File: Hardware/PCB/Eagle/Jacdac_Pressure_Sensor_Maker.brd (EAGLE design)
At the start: 27.9 x 27.9 mm, 31 parts, among them J1 JACDAC_EDGE_CONN-INNIE, J2 SWD-ADAPTER-, J3 HEADER_MALE-1X07, U1 NCP114ASN330T1G, U2 STM32F042F6P6, U3 BAT54S,235, U4 LPS33HWTR

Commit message: Corrected Capacitor values
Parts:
- C5: value 33pF -> 1uF
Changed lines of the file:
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@@
 <attribute name="NAME" x="14.224" y="8.382" size="0.8128" layer="25" ratio="15" rot="R90" align="bottom-center"/>
 </element>
-<element name="C5" library="milador_SMD" library_urn="urn:adsk.eagle:library:27847482" package="0805-MP" package3d_urn="urn:adsk.eagle:package:27847629/3" value="33pF" x="15.24" y="13.462" smashed="yes">
+<element name="C5" library="milador_SMD" library_urn="urn:adsk.eagle:library:27847482" package="0805-MP" package3d_urn="urn:adsk.eagle:package:27847629/3" value="1uF" x="15.24" y="13.462" smashed="yes">
 <attribute name="NAME" x="12.8524" y="12.9286" size="0.8128" layer="25" font="vector" ratio="15" align="bottom-center"/>
 <attribute name="VALUE" x="13.0302" y="12.4968" size="0.8128" layer="27" font="vector" ratio="15" align="top-center"/>

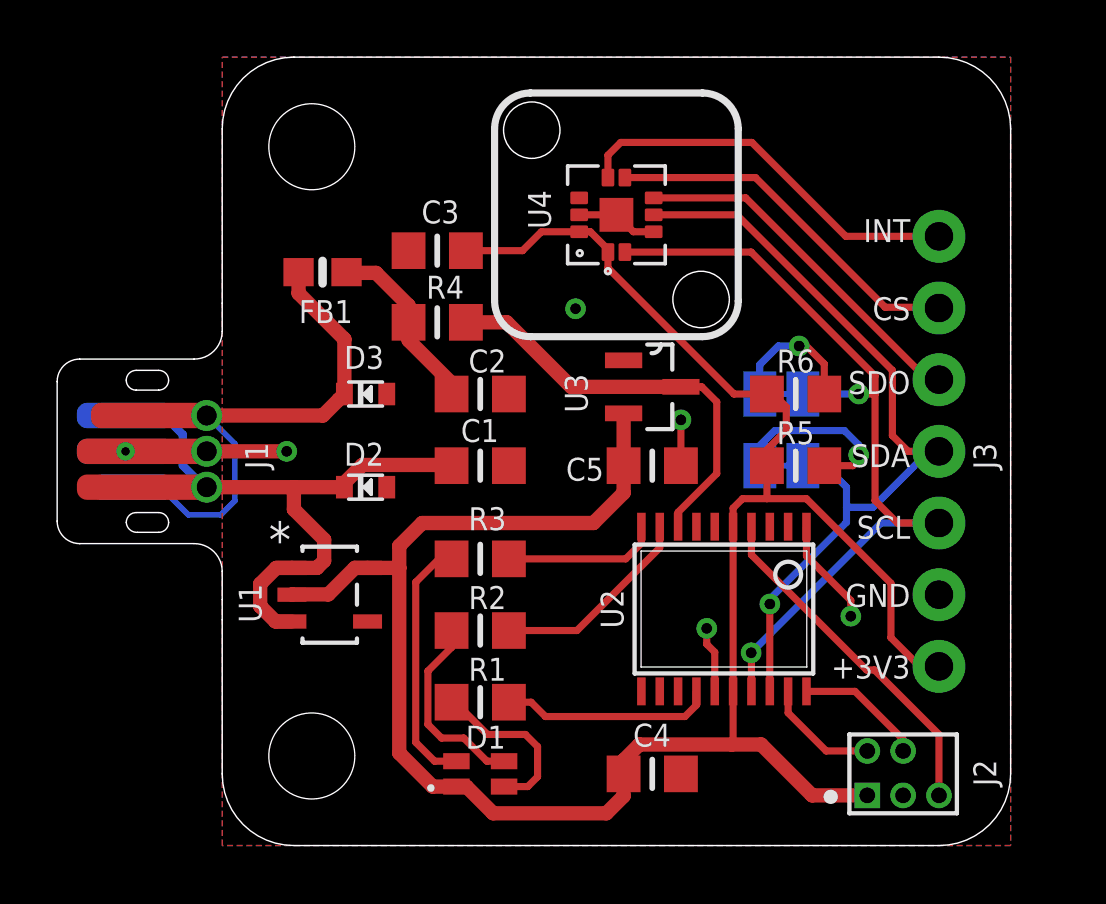
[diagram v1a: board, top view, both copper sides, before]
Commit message: Updated design : Centered Pressure Sensor
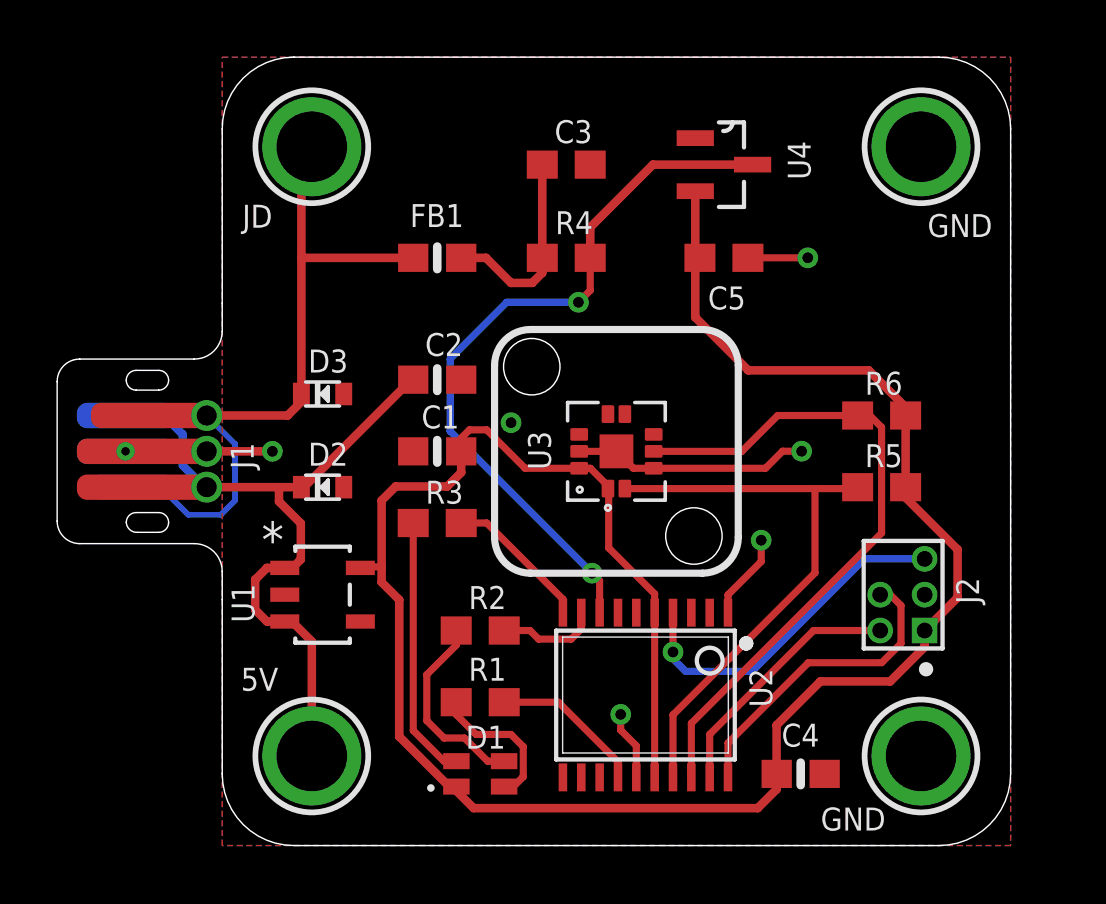
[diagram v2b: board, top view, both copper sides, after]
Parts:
- removed J3: HEADER_MALE-1X07, milador:HEADER_MALE-1X07
- removed JP3: STAND-OFF-3.0, milador:STAND-OFF-3.0
- removed SJ1, SJ2: (no value), milador_SMD:SOLDERJUMPER_CLOSEDWIRE
- removed U$2: MILADOR-PIN-NAME-SCK, milador:PIN-SCK
- removed U$3: MMC-LOGO-SM, MMC Eagle:MMC_SMALL_LOGO
- added H1, H3, H4: MOUNTINGHOLE2.5, milador:MOUNTINGHOLE_2.5_PLATED
- added MMC_LOGO: MMC_LOGO-SM, MMC Eagle:MMC_SMALL_LOGO
- C1: value 1uF -> 0.1uF; device milador_SMD:0805-MP -> milador_SMD:0603-NO
- C2: value 33pF -> 1uF; device milador_SMD:0805-MP -> milador_SMD:0603-NO
- C3: value 0.1uF -> 33pF; device milador_SMD:0805-MP -> milador_SMD:0603
- C4: device milador_SMD:0805-MP -> milador_SMD:0603-NO
- C5, R1, R2, R3, R4, R5, R6: device milador_SMD:0805-MP -> milador_SMD:0603
- H2: value STAND-OFF-3.0 -> MOUNTINGHOLE2.5; device milador:STAND-OFF-3.0 -> milador:MOUNTINGHOLE_2.5_PLATED
- U$1: value MILADOR-PIN-NAME-SDA -> JACDAC-DEVICE-LPS33HW; device milador:PIN-SDA -> milador:JACDAC-LPS33HW
- U3: value BAT54S,235 -> LPS33HWTR; device milador_SMD:SOT23-3 -> milador_SMD:PQFN60P330X330X290-11N
- U4: value LPS33HWTR -> BAT54S,235; device milador_SMD:PQFN60P330X330X290-11N -> milador_SMD:SOT23-3
- moved LABEL2 16.4 mm to (23.1, 18.6)
- moved C5 7.79 mm to (17.8, 20.8)
- moved U$1 6.55 mm to (18.7, 19.8)
- moved J2 6.19 mm to (24.9, 7.62), turned to 90 degrees
- moved C3 5.49 mm to (12.2, 24.1), turned to 0 degrees
- moved C4 5.26 mm to (20.5, 2.54)
- moved R4 5.11 mm to (12.2, 20.8)
- moved U4 4.20 mm to (17.8, 24.1), turned to 0 degrees
- moved U2 4.13 mm to (15.0, 5.33)
- moved FB1 4.10 mm to (7.62, 20.8)
- moved R5 3.14 mm to (23.4, 12.7), turned to 0 degrees
- moved R6 3.14 mm to (23.4, 15.2), turned to 0 degrees
- moved U3 2.62 mm to (14.0, 14.0), turned to 90 degrees
- moved R3 1.98 mm to (7.62, 11.4)
- moved C2 1.61 mm to (7.62, 16.5)
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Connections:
- removed net CS: J3.6, U4.6
- removed net INT: J3.7, U4.7
- removed net N$6: R6.1, SJ1.2
- removed net N$7: R5.1, SJ2.2
- removed net SDO: J3.5, U4.5
- net +3V3: now also C1.1, U3.1, U3.10, U4.2; no longer C3.1, J3.1, U1.2, U3.2, U4.1, U4.10
- net GND: now also H3.P$1, H4.P$1, U1.2, U3.3, U3.8, U3.9, U3.EP, U4.1; no longer J3.2, U3.1, U4.3, U4.8, U4.9, U4.EP
- net JD_DATA: now also U4.3; no longer U3.3
- net J_DATA: now also H2.P$1
- net N$4: now also C3.1; no longer C2.1
- net SCL: now also R5.1, U3.2; no longer J3.3, SJ1.1, U4.2
- net SDA: now also R6.1, U3.4; no longer J3.4, SJ2.1, U4.4
- net VCC: now also C2.1, H1.P$1; no longer C1.1
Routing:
- net INT: track 14.1 -> 0.00 mm
- net CS: track 13.0 -> 0.00 mm
- net SDO: track 12.8 -> 0.00 mm
- net JD_DATA: track 15.0 -> 26.1 mm, vias 0 -> 2
- net SCL: track 30.2 -> 20.6 mm, vias 2 -> 0
- net J_DATA: track 19.8 -> 26.3 mm
- net SWCLK: track 4.54 -> 11.0 mm
- net N$7: track 6.48 -> 0.00 mm, vias 1 -> 0
- net SDA: track 29.3 -> 24.0 mm, vias 1 -> 0
- net SWDIO: track 4.13 -> 9.09 mm
- net GND: track 16.4 -> 21.4 mm, vias 5 -> 6
- net N$6: track 4.93 -> 0.00 mm, vias 1 -> 0
- net VCC: track 23.7 -> 28.1 mm
- net RGB_G: track 7.31 -> 3.58 mm
- net +3V3: track 80.6 -> 77.9 mm
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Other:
- outline, holes or cut-outs redrawn
- board text added: "5V"
- board text added: "JD"
- board text removed: "+3V3"
- board text removed: "CS"
- board text removed: "INT"
- board text removed: "SCL"
- board text removed: "SDA"
- board text removed: "SDO"

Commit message: Added version 1.0
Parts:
- removed D2, D3: RCLAMP0521PATCT, milador_SMD:SOD-523
- removed H1, H2, H3, H4: MOUNTINGHOLE2.5, milador:MOUNTINGHOLE_2.5_PLATED
- removed J1: JACDAC_EDGE_CONN-INNIE, Jacdac:JACDAC-EDGE-CONN-INNIE
- removed LABEL2: JACDAC-DEVICE-PS, milador:JACDAC-PRESSURE-SENSOR
- removed LABEL3: MILADOR-LOGO-, milador:MILADOR_LOGO1
- removed U$1: JACDAC-DEVICE-LPS33HW, milador:JACDAC-LPS33HW
- added J3: 5V, milador:M3-HOLE-PWR-OUTL
- added J4: DATA, milador:M3-HOLE-DATA-NOTCH
- added J5, J6: GND, milador:M3-HOLE-GND
- added JD1, JD2: JACDAC-EDGE-OUTIE, milador:JD-EDGE-OUTIE
- added LABEL_JACDAC_PS: MILADOR-JACDAC-DEVICE-PS, milador:JACDAC-PRESSURE-SENSOR
- added LABEL_LPS33HW: MILADOR-JACDAC-DEVICE-LPS33HW, milador:JACDAC-LPS33HW
- added LABEL_MILADOR: MILADOR-LOGO-, milador:MILADOR_LOGO1
- added LABEL_QR_CODE: MILADOR-QR-CODE-JACDAC-GITHUB-PS, milador:MILADOR_QR_JACDAC_PS
- C1: value 0.1uF -> 1uF
- C2: value 1uF -> 33pF; device milador_SMD:0603-NO -> milador_SMD:0603
- C3: value 33pF -> 1uF; device milador_SMD:0603 -> milador_SMD:0603-NO
- C4: value 1uF -> 0.1uF
- MMC_LOGO: value MMC_LOGO-SM -> MMC_LOGO-XSM; device MMC Eagle:MMC_SMALL_LOGO -> MMC Eagle:MMC_X-SMALL_LOGO
- U1: value NCP114ASN330T1G -> STM32F042F6P6; device milador_SMD:TSOP-5_ONS -> milador_SMD:TSSOP20
- U2: value STM32F042F6P6 -> NCP114ASN330T1G; device milador_SMD:TSSOP20 -> milador_SMD:TSOP-5_ONS
- moved C3 21.8 mm to (17.8, 3.00), turned to 270 degrees
- moved R1 12.1 mm to (9.80, 17.2)
- moved R2 12.1 mm to (9.80, 19.7)
- moved D1 12.0 mm to (9.30, 14.5)
- moved R3 11.0 mm to (9.80, 22.2)
- moved U1 10.1 mm to (12.8, 4.75), turned to 180 degrees
- moved MMC_LOGO 9.48 mm to (12.0, 4.50), turned to 0 degrees
- moved C4 9.13 mm to (18.8, 11.5)
- moved C1 8.49 mm to (8.25, 5.50), turned to 90 degrees
- moved U2 7.90 mm to (9.50, 11.0), turned to 90 degrees
- moved C2 7.42 mm to (14.0, 20.3)
- moved FB1 6.55 mm to (13.8, 23.0)
- moved R6 5.27 mm to (18.5, 17.2)
- moved J2 5.18 mm to (19.9, 6.25)
- moved R5 4.96 mm to (18.8, 14.5)
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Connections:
- net +3V3: now also C3.1, U1.16; no longer C1.1, U2.16
- net GND: now also J5.H, J6.H, JD1.2, JD1.5, JD1.P$2, JD1.P$4, JD2.2, JD2.5, JD2.P$2, JD2.P$4, U1.1, U1.15, U2.2; no longer D2.1, D3.1, H3.P$1, H4.P$1, J1.GND1, J1.GND2, J1.GND3, J1.GND4, U1.2, U2.1, U2.15
- net JD_DATA: now also U1.8; no longer U2.8
- net J_DATA: now also J4.H, JD1.1, JD1.6, JD1.P$3, JD2.1, JD2.6, JD2.P$3; no longer D3.2, H2.P$1, J1.JD1, J1.JD2, J1.JD3
- net N$4: now also C2.1; no longer C3.1
- net RESET: now also U1.4; no longer U2.4
- net RGB_B: now also U1.14; no longer U2.14
- net RGB_G: now also U1.10; no longer U2.9
- net RGB_R: now also U1.9; no longer U2.10
- net SCL: now also U1.17; no longer U2.17
- net SDA: now also U1.18; no longer U2.18
- net SWCLK: now also U1.20; no longer U2.20
- net SWDIO: now also U1.19; no longer U2.19
- net VCC: now also C1.1, J3.H, JD1.3, JD1.4, JD1.P$1, JD2.3, JD2.4, JD2.P$1, U2.1, U2.3; no longer C2.1, D2.2, H1.P$1, J1.VDD1, J1.VDD2, J1.VDD3, U1.1, U1.3
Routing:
- net GND: track 21.4 -> 104.8 mm, vias 6 -> 9
- net +3V3: track 77.9 -> 47.4 mm, vias 0 -> 2
- net J_DATA: track 26.3 -> 51.3 mm, vias 0 -> 5
- net VCC: track 28.1 -> 48.4 mm
- net RGB_R: track 5.20 -> 21.0 mm, vias 0 -> 2
- net RGB_G: track 3.58 -> 17.4 mm, vias 0 -> 2
- net RGB_B: track 5.46 -> 17.7 mm, vias 0 -> 2
- net JD_DATA: track 26.1 -> 19.9 mm
- net RESET: track 12.4 -> 7.22 mm
- net SWCLK: track 11.0 -> 6.95 mm
- net SWDIO: track 9.09 -> 6.46 mm, vias 0 -> 1
- net SDA: track 24.0 -> 21.9 mm, vias 0 -> 2
- net SCL: track 20.6 -> 18.7 mm, vias 0 -> 2
- net N$4: track 7.22 -> 5.92 mm
- net N$3: track 9.33 -> 8.29 mm
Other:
- board size 27.9 x 27.9 mm -> 25 x 25 mm
- board text added: "V1.1"
- board text removed: "5V"
- board text removed: "JD"
